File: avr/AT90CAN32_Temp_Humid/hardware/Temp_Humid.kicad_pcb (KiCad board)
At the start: 2 copper layers, 56.1 x 48.3 mm, 23 parts, among them K1 CONN_3, P1 CONN_3X2, P2 CONN_4, P3 CONN_4, SW1 SW_PUSH, U1 DS1820, U2 AT90CAN32, U3 7805, U4 MCP2551, U5 HIH4000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

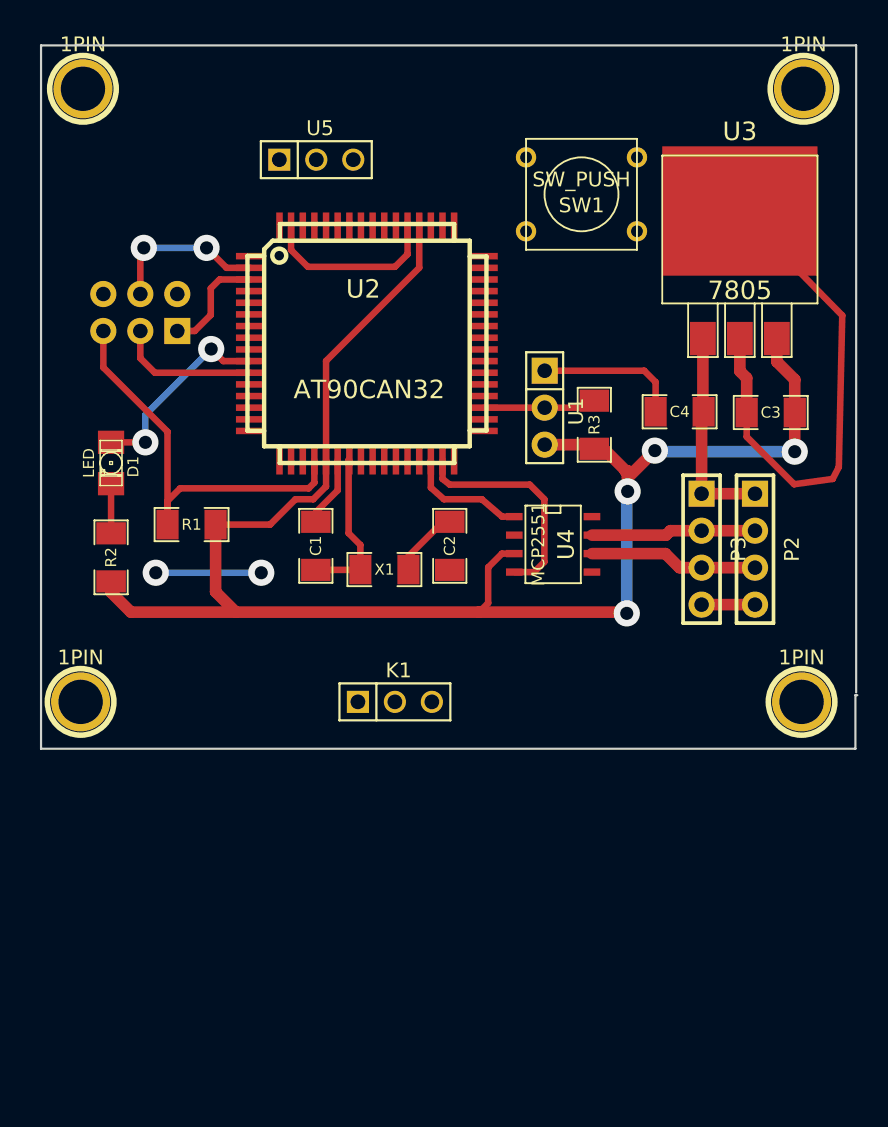
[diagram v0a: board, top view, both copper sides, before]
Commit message: Updating PCB before footprint test on paper printout
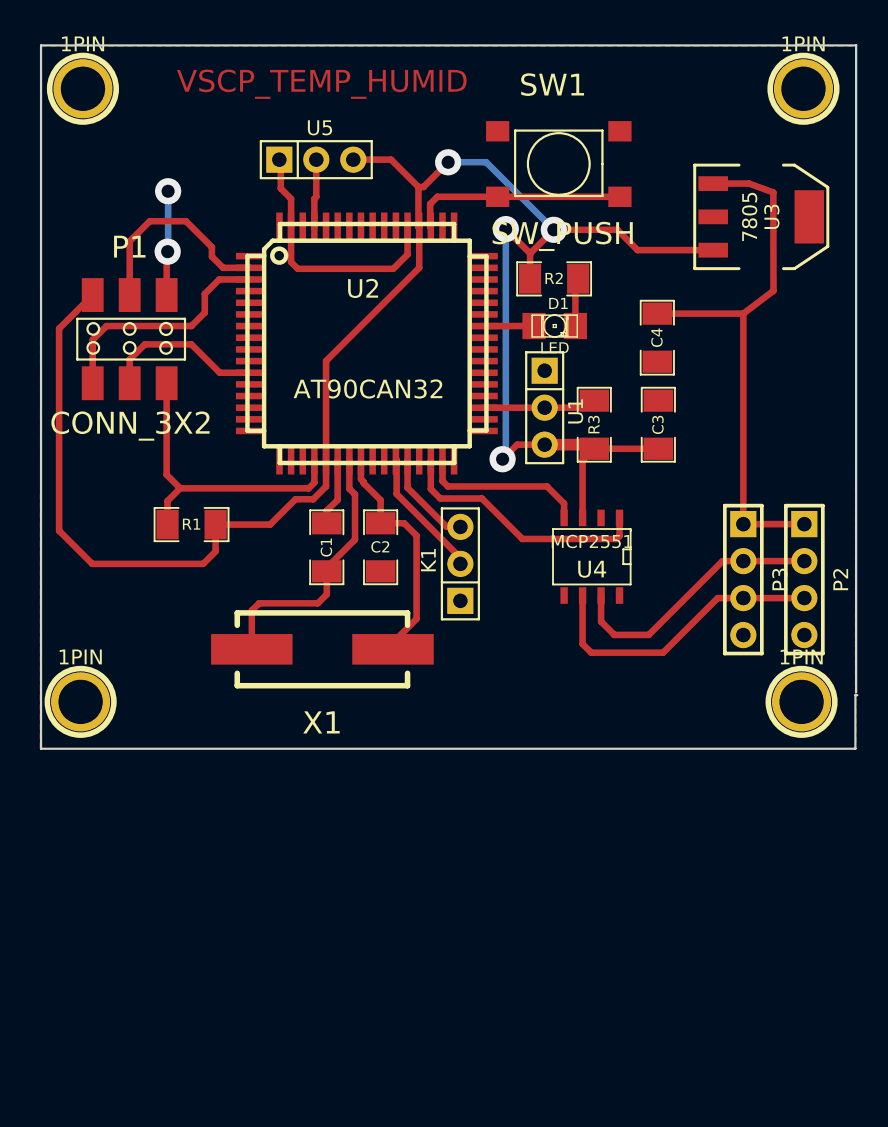
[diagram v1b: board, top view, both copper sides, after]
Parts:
- P1: footprint pin_array_3x2 -> Pin_2x3_smd; moved to F.Cu
- SW1: footprint SW_PUSH_SMALL -> Switch_SPC
- U3: footprint DPAK3 -> SOT223
- X1: footprint SM1206 -> Crystal_HC49-SD_SMD_RevA_09Aug2010
- moved R2 36.0 mm to (179.4, 92.0), turned to 0 degrees
- moved D1 31.9 mm to (179.5, 95.3), turned to 0 degrees
- moved K1 10.5 mm to (173.0, 111.6), turned to 90 degrees
- moved U3 8.49 mm to (193.7, 87.8), turned to 270 degrees
- moved C3 7.77 mm to (186.6, 102.1), turned to 90 degrees
- moved X1 6.94 mm to (163.5, 117.5)
- moved C4 5.31 mm to (186.5, 96.1), turned to 270 degrees
- moved C2 4.75 mm to (167.5, 110.5)
- moved P2 3.98 mm to (196.6, 112.7)
- moved P3 3.55 mm to (192.4, 112.7)
- moved U4 2.79 mm to (182.0, 111.1), turned to 180 degrees
- moved SW1 2.60 mm to (179.8, 84.2)
- moved P1 1.97 mm to (150.3, 96.2)
- moved C1 0.76 mm to (163.8, 110.5)
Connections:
- D1 pad 1: N-0000024 -> N-0000017
- U2 pad 10: N-0000024 -> (no net)
- U2 pad 42: (no net) -> N-0000017
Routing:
- net GND: track 66.4 -> 29.8 mm, vias 0 -> 2
- net +12V: track 14.4 -> 38.2 mm
- net N-0000015: track 0.00 -> 14.9 mm
- net N-0000024: track 13.7 -> 0.00 mm, vias 2 -> 0
- net +5V: track 116.9 -> 130.3 mm
- net N-0000032: track 4.73 -> 16.2 mm
- net N-000001: track 8.38 -> 17.7 mm
- net N-0000018: track 0.00 -> 9.00 mm
- net N-000003: track 11.6 -> 20.4 mm
- net /PE1: track 7.57 -> 16.3 mm
- net (no net): track 7.75 -> 0.00 mm, vias 2 -> 0
- net N-000009: track 28.9 -> 21.4 mm
- net N-0000031: track 11.0 -> 18.5 mm
- net N-000005: track 11.3 -> 18.2 mm
- net N-0000019: track 0.00 -> 6.65 mm
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- added copper zone on F.Cu, net GND
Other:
- board text added: "VSCP_TEMP_HUMID"

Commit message: Last update on PCB before ordering
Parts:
- removed P2, P3: CONN_4, PIN_ARRAY_4x1
- added C5: 100nF, SM1206, F.Cu at (170.7, 83.0)
- added C6: 100nF, SM1206, F.Cu at (159.9, 110.5)
- added U6: RJ45_DUAL, RJ45_DUAL, F.Cu at (168.1, 130.2)
- moved U3 31.8 mm to (185.6, 118.6), turned to 0 degrees
- moved C4 30.4 mm to (183.4, 126.3)
- moved C3 24.3 mm to (187.9, 126.3), turned to 270 degrees
- moved 1PIN 23.5 mm to (191.0, 144.0)
- moved 1PIN 22.9 mm to (146.0, 144.0)
- moved 1PIN 5.67 mm to (191.0, 80.0)
- moved U4 5.47 mm to (178.2, 115.0)
- moved R3 2.11 mm to (183.4, 100.4), turned to 270 degrees
- moved 1PIN 1.48 mm to (146.0, 80.0)
- moved U1 1.03 mm to (179.6, 101.5), turned to 90 degrees
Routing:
- net GND: track 29.8 -> 109.9 mm, vias 2 -> 8
- net +5V: track 130.3 -> 160.5 mm, vias 4 -> 0
- net N-0000014: track 18.2 -> 35.5 mm
- net N-000006: track 20.4 -> 33.7 mm
- net +12V: track 38.2 -> 44.8 mm, vias 0 -> 3
- net N-000001: track 17.7 -> 19.3 mm
- net N-0000021: track 7.83 -> 9.33 mm
- net /PD1: track 14.3 -> 13.1 mm
- added copper zone on B.Cu, net GND
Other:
- board outline removed
- board text added: "VSCP TEMP_HUMID"
- board text removed: "VSCP_TEMP_HUMID"

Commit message: Trying to fix sendVSCPFrame
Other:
- board outline added: 50.2 x 69.2 mm
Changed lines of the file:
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@@
     (links 67)
     (no_connects 0)
-    (area 140.205714 76.017 193.780001 147.825)
+    (area 140.205714 77.179999 193.780001 147.729)
     (thickness 1.6)
     (drawings 7)
@@
     (trace_min 0.254)
     (segment_width 0.2)
-    (edge_width 0.15)
+    (edge_width 0.2)
     (via_size 1.8)
     (via_drill 1)
@@
     (visible_elements FFFFFFBF)
     (pcbplotparams
-      (layerselection 32769)
-      (usegerberextensions false)
+      (layerselection 284196865)
+      (usegerberextensions true)
       (excludeedgelayer true)
       (linewidth 0.150000)
@@
       (padsonsilk false)
       (subtractmaskfromsilk false)
-      (outputformat 2)
+      (outputformat 1)
       (mirror false)
-      (drillshape 2)
+      (drillshape 0)
       (scaleselection 1)
       (outputdirectory ""))
@@
     (tags DEV)
     (path 1pin)
-    (fp_text reference 1PIN (at 0 -3.048) (layer F.SilkS)
+    (fp_text reference 1PIN (at -5.64 -0.78) (layer F.SilkS)
       (effects (font (size 1.016 1.016) (thickness 0.254)))
     )
@@
     (tags DEV)
     (path 1pin)
-    (fp_text reference 1PIN (at 0 -3.048) (layer F.SilkS)
+    (fp_text reference 1PIN (at 5.82 -0.4) (layer F.SilkS)
       (effects (font (size 1.016 1.016) (thickness 0.254)))
     )
@@
   (module RJ45_DUAL (layer F.Cu)
     (at 168.08 130.19)
-    (fp_text reference U6 (at 0 16.51) (layer F.SilkS)
+    (fp_text reference U6 (at -13.93 -5.18) (layer F.SilkS)
       (effects (font (size 1.5 1.5) (thickness 0.15)))
     )
@@
     )
   )
-  (gr_line (start 143.48 146.43) (end 143.48 144.27) (angle 90) (layer Eco2.User) (width 0.2))
-  (gr_line (start 193.68 146.46) (end 193.68 144.27) (angle 90) (layer Eco2.User) (width 0.2))
-  (gr_line (start 143.48 146.46) (end 193.68 146.46) (angle 90) (layer Eco2.User) (width 0.2))
-  (gr_line (start 143.48 144.3) (end 143.48 77.28) (angle 90) (layer Eco2.User) (width 0.2))
-  (gr_line (start 193.68 77.28) (end 193.68 144.3) (angle 90) (layer Eco2.User) (width 0.2))
-  (gr_line (start 143.48 77.28) (end 193.68 77.28) (angle 90) (layer Eco2.User) (width 0.2))
+  (gr_line (start 143.48 146.43) (end 143.48 144.27) (angle 90) (layer Edge.Cuts) (width 0.2))
+  (gr_line (start 193.68 146.46) (end 193.68 144.27) (angle 90) (layer Edge.Cuts) (width 0.2))
+  (gr_line (start 143.48 146.46) (end 193.68 146.46) (angle 90) (layer Edge.Cuts) (width 0.2))
+  (gr_line (start 143.48 144.3) (end 143.48 77.28) (angle 90) (layer Edge.Cuts) (width 0.2))
+  (gr_line (start 193.68 77.28) (end 193.68 144.3) (angle 90) (layer Edge.Cuts) (width 0.2))
+  (gr_line (start 143.48 77.28) (end 193.68 77.28) (angle 90) (layer Edge.Cuts) (width 0.2))
   (gr_text "VSCP\nTEMP_HUMID" (at 147.32 121.11 90) (layer F.Cu)
     (effects (font (size 1.5 1.5) (thickness 0.3)))
